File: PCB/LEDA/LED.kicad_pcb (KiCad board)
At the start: 2 copper layers, 70 x 70 mm, 26 parts, among them J1 USB_A, J2 Conn_01x03, J3 TC2030-USB-NL-DS, U1 ICS43434_MEMS_Mic, U2 ESP32-S3-MINI-1, U5 MD8942

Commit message: Latest layout
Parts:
- removed ?: , clipboard:8abff937-711c-455e-bc8a-c75c5e04b52f
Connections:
- J3 pad 2: DC -> D-
- J3 pad 6: GND -> D-
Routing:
- net GND: track 10.8 -> 15.5 mm, vias 9 -> 10
- net DC: track 46.2 -> 49.2 mm

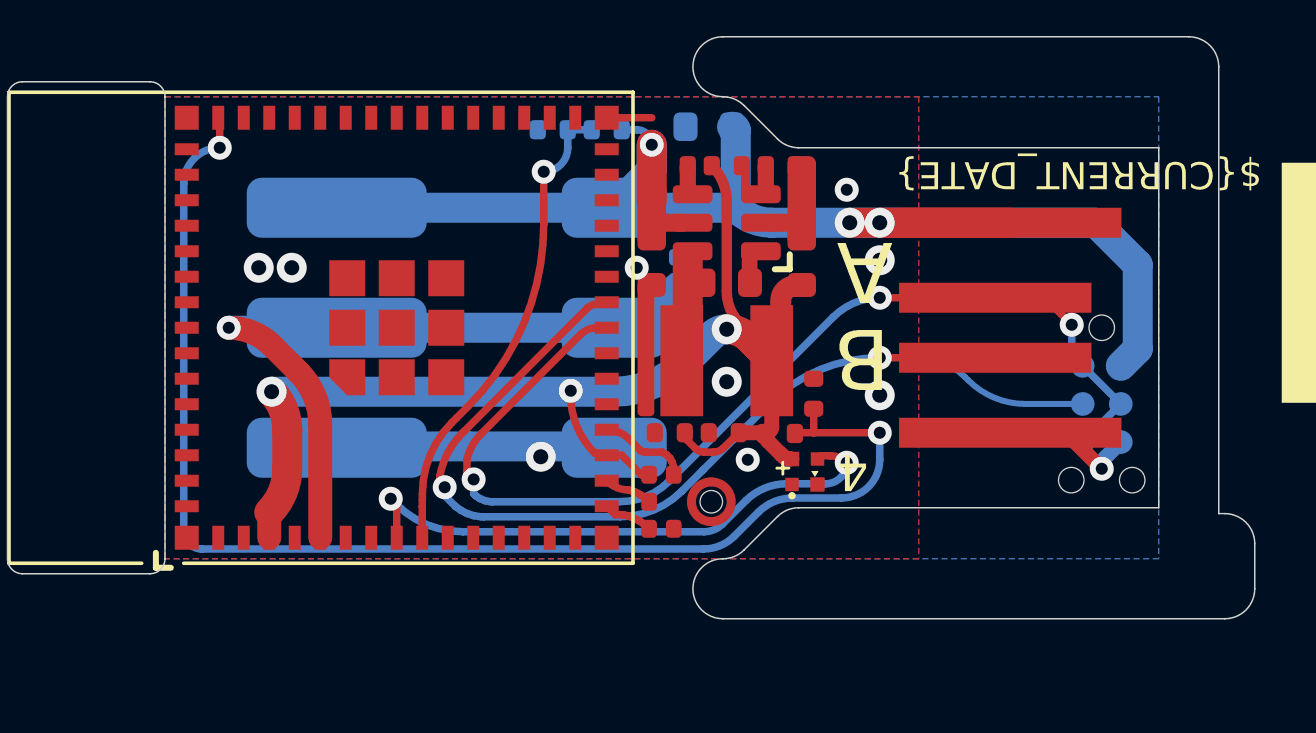
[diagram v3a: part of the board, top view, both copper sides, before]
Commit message: New LEDs
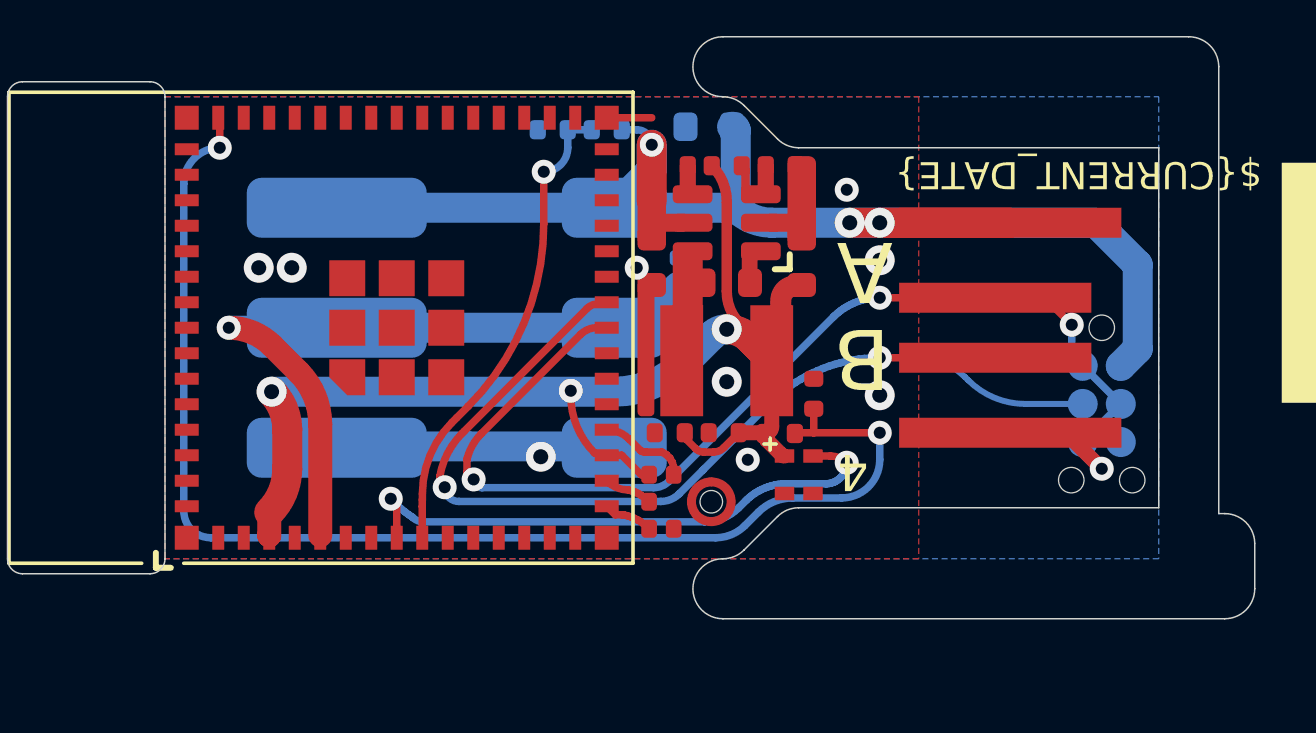
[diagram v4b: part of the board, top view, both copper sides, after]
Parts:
- D1: footprint RevK:SMD1010 -> RevK:SMD1615
- moved D1 0.22 mm to (109.0, 104.9)
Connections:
- D1 pad 1: unconnected-(D1-O-Pad1) -> GND
- D1 pad 2: +3.3V -> LED1
- D1 pad 3: GND -> +3.3V
- D1 pad 4: LED1 -> unconnected-(D1-O-Pad4)
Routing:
- net GND: track 15.5 -> 14.3 mm
- net Net-(U2-EN): track 43.8 -> 43.2 mm
- net D-: track 36.0 -> 35.5 mm

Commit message: Not a good case, but started one, and some cleaner renders
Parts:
- J2: footprint RevK:WAGO-2060-453-998-404 -> RevK:WAGO-2060-453-998-404-O
